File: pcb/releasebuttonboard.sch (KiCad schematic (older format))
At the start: 10 parts

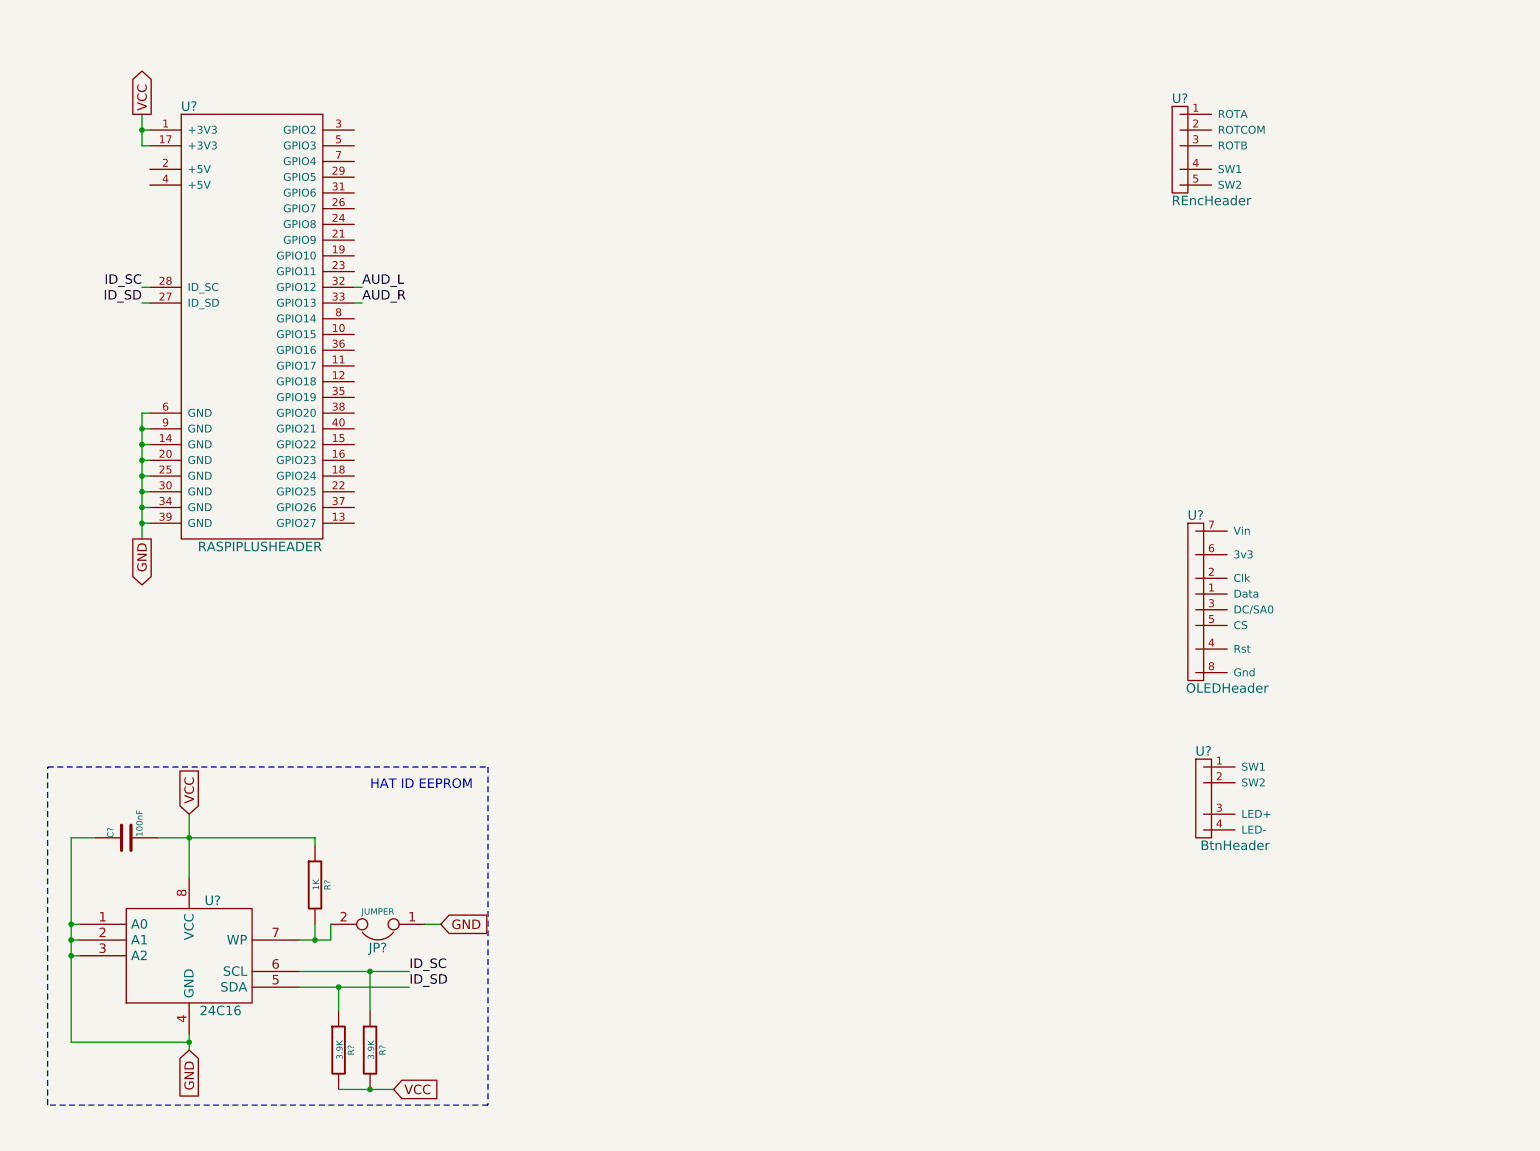
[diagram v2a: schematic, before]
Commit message: Audio output circuit.
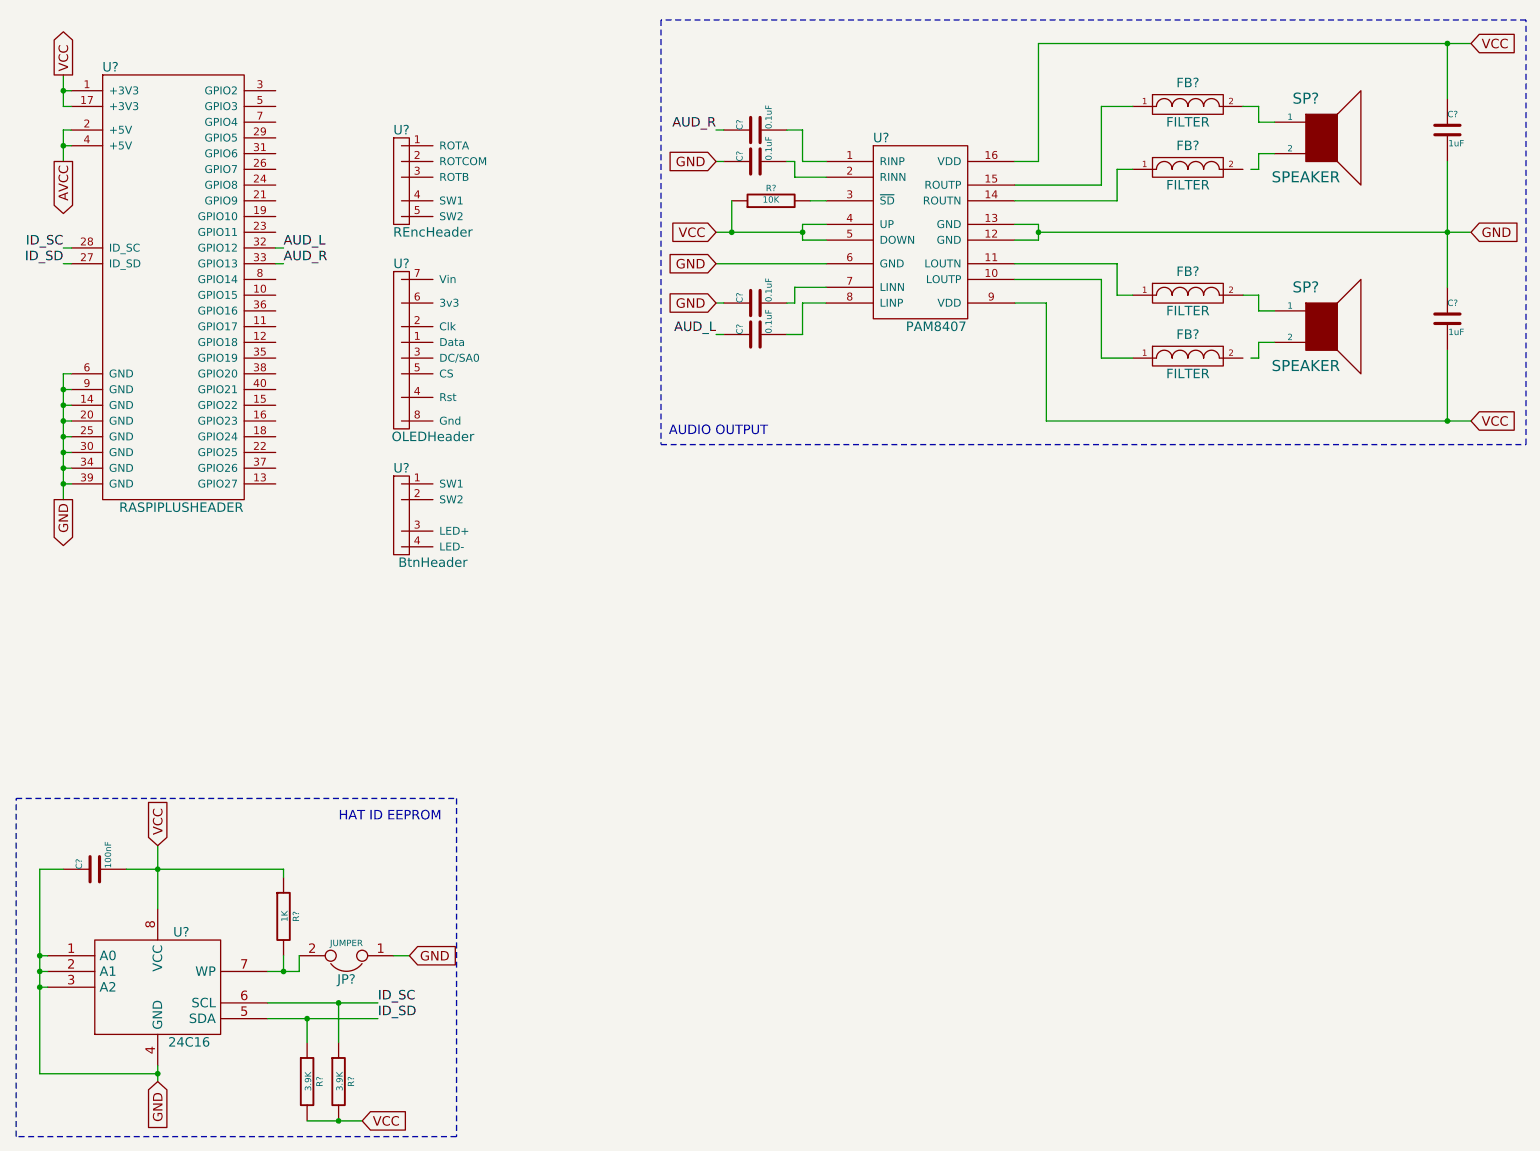
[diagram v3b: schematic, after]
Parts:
- added C? (x2): 1uF, symbol C
- added C? (x4): 0.1uF, symbol C
- added FB? (x4): FILTER, symbol FILTER
- added R?: 10K, symbol R
- added SP? (x2): SPEAKER, symbol SPEAKER
- added U?: PAM8407, symbol PAM8407
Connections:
- net AUD_L: now also C?.1
- net AUD_R: now also C?.1
- net GND: now also C?.1, C?.1, C?.1, C?.2, U?.12 (GND), U?.13 (GND), U?.6 (GND)
- net VCC: now also C?.1, C?.2, R?.1, U?.16 (VDD), U?.4 (UP), U?.5 (DOWN), U?.9 (VDD)
- net AVCC: now reaches U?.2 (+5V)
- net AVCC: now also U?.4 (+5V)
- new net: FB?.1, U?.15 (ROUTP)
- new net: FB?.2, SP?.1 (x2)
- new net: FB?.1, U?.14 (ROUTN)
- new net: C?.2, U?.1 (RINP)
- new net: FB?.1, U?.10 (LOUTP)
- new net: FB?.1, U?.11 (LOUTN)
- new net: C?.2, U?.2 (RINN)
- new net: R?.2, U?.3 (~SD)
- new net: C?.2, U?.7 (LINN)
- new net: C?.2, U?.8 (LINP)
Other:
- note added: "AUDIO OUTPUT"
- moved on the sheet: C?, JP?, R?, U?

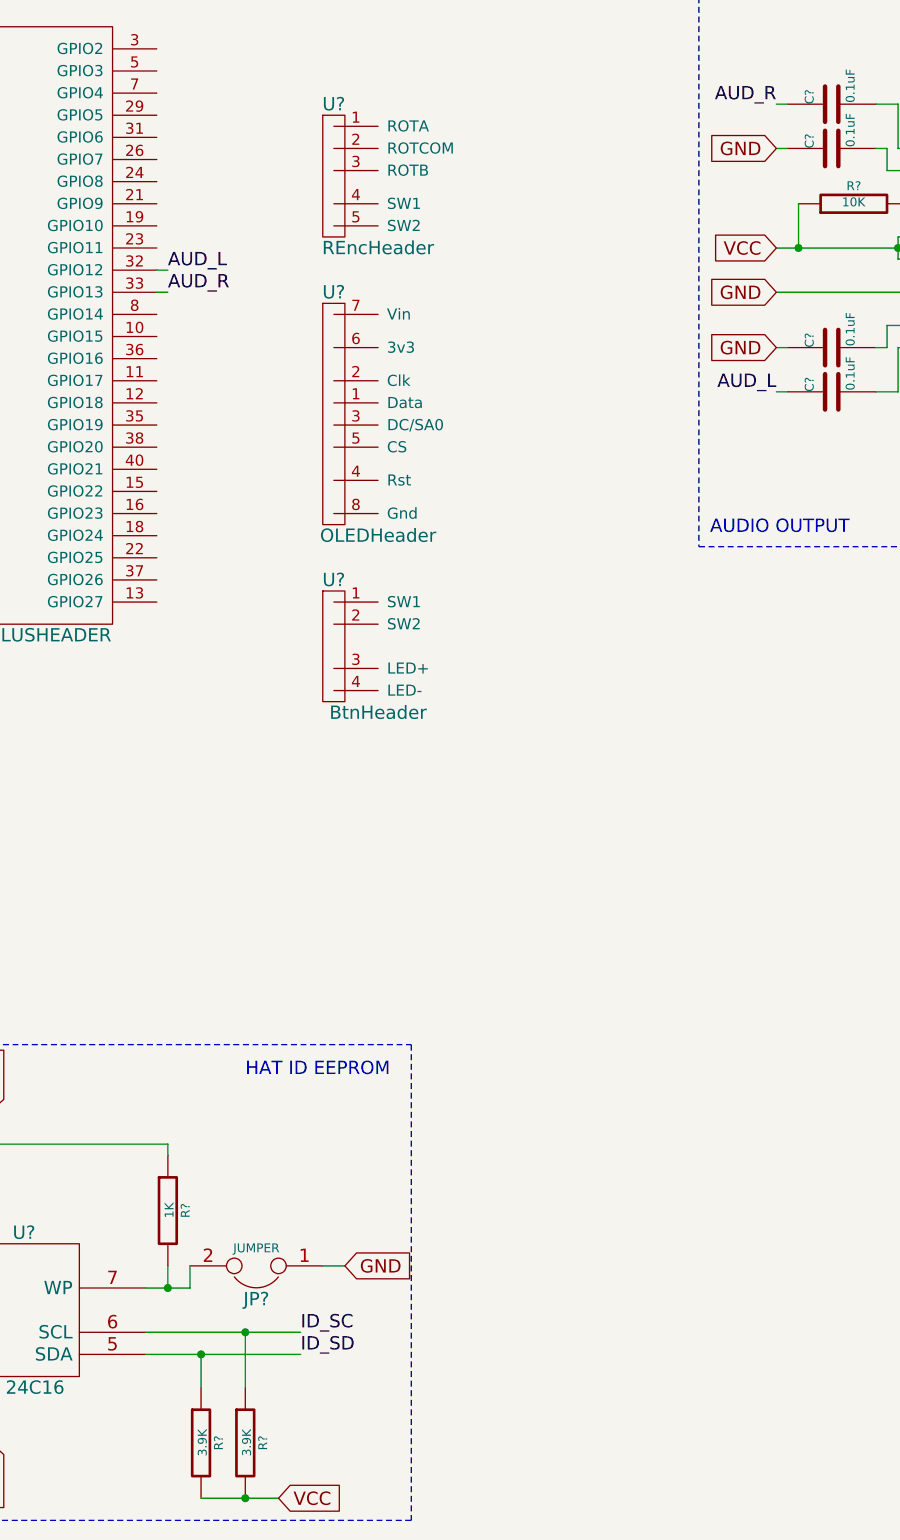
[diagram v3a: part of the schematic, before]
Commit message: Connect OLED header to Raspberry Pi IO pins.
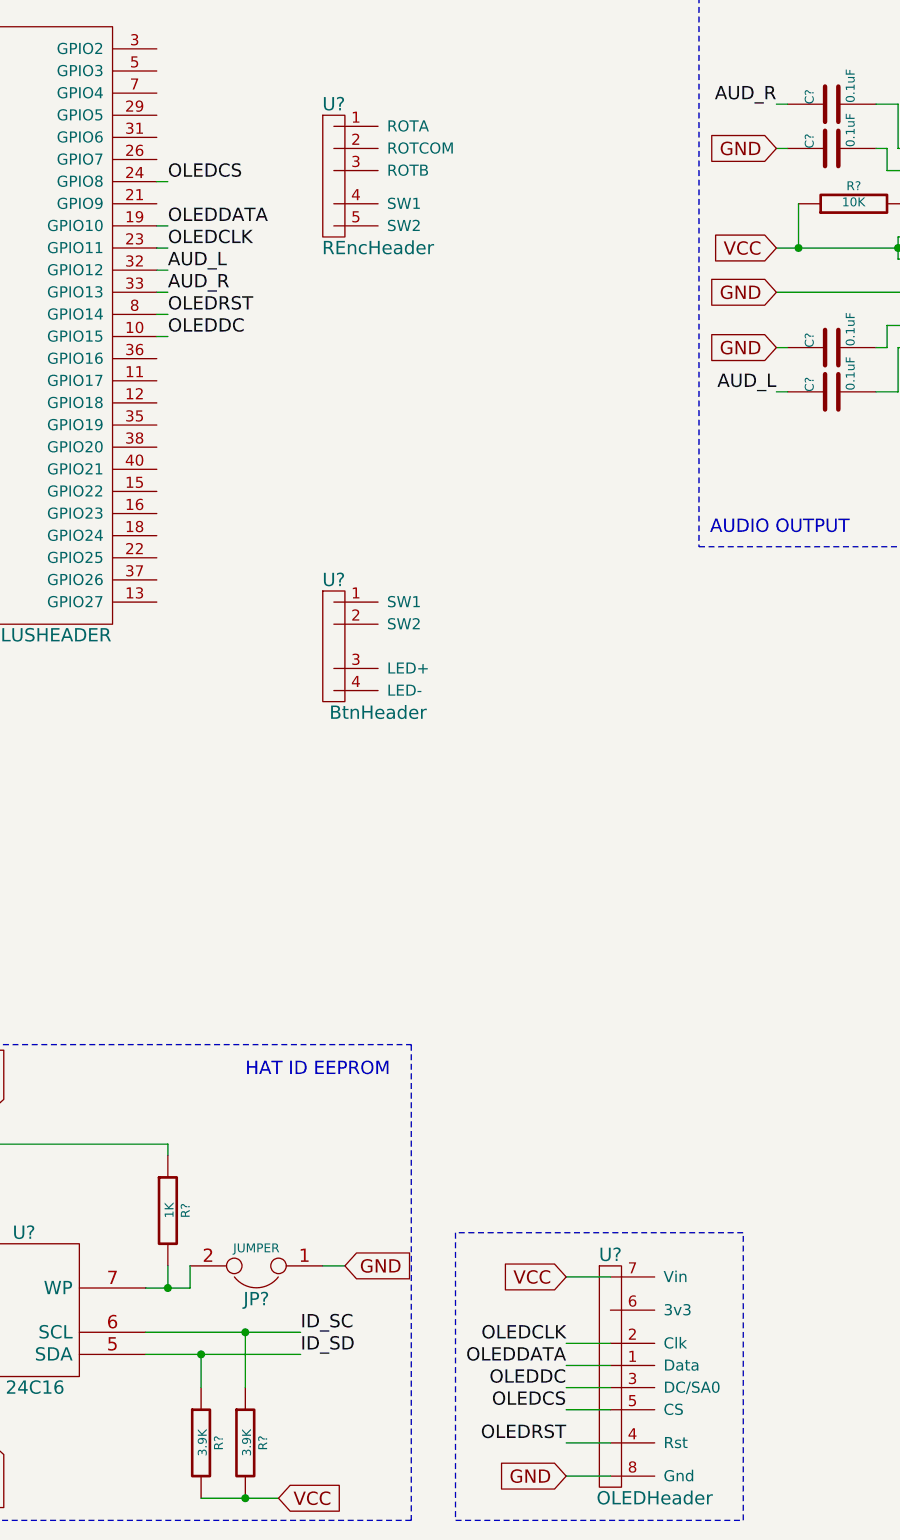
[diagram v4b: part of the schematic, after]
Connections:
- net GND: now also U?.8 (Gnd)
- net VCC: now also U?.7 (Vin)
- net OLEDDC: now reaches U?.10 (GPIO15)
- net OLEDDC: now also U?.3 (DC/SA0)
- net OLEDDATA: now reaches U?.19 (GPIO10)
- net OLEDDATA: now also U?.1 (Data)
- net OLEDCLK: now reaches U?.23 (GPIO11)
- net OLEDCLK: now also U?.2 (Clk)
- net OLEDCS: now reaches U?.24 (GPIO8)
- net OLEDCS: now also U?.5 (CS)
- net OLEDRST: now reaches U?.8 (GPIO14)
- net OLEDRST: now also U?.4 (Rst)
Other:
- moved on the sheet: U?
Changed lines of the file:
@@
 L OLEDHeader U?
 U 1 1 54A7A9C0
-P 3150 2750
-F 0 "U?" H 3150 3250 60  0000 C CNN
-F 1 "OLEDHeader" H 3350 2150 60  0000 C CNN
-F 2 "" H 3150 2950 60  0000 C CNN
-F 3 "" H 3150 2950 60  0000 C CNN
-	1    3150 2750
+P 4400 7100
+F 0 "U?" H 4400 7600 60  0000 C CNN
+F 1 "OLEDHeader" H 4600 6500 60  0000 C CNN
+F 2 "" H 4400 7300 60  0000 C CNN
+F 3 "" H 4400 7300 60  0000 C CNN
+	1    4400 7100
 	1    0    0    -1
 $EndComp
@@
 Text Notes 4850 3350 0    60   ~ 0
 AUDIO OUTPUT
+Text GLabel 4200 7600 0    60   Input ~ 0
+GND
+Text GLabel 4200 6700 0    60   Input ~ 0
+VCC
+Text Label 4200 7000 2    60   ~ 0
+OLEDCLK
+Text Label 4200 7100 2    60   ~ 0
+OLEDDATA
+Text Label 4200 7200 2    60   ~ 0
+OLEDDC
+Text Label 4200 7300 2    60   ~ 0
+OLEDCS
+Text Label 4200 7450 2    60   ~ 0
+OLEDRST
+Wire Wire Line
+	4200 6700 4400 6700
+Wire Wire Line
+	4200 7000 4400 7000
+Wire Wire Line
+	4200 7100 4400 7100
+Wire Wire Line
+	4200 7200 4400 7200
+Wire Wire Line
+	4200 7300 4400 7300
+Wire Wire Line
+	4200 7450 4400 7450
+Wire Wire Line
+	4200 7600 4400 7600
+Wire Notes Line
+	3700 6500 3700 7800
+Wire Notes Line
+	3700 7800 5000 7800
+Wire Notes Line
+	5000 7800 5000 6500
+Wire Notes Line
+	5000 6500 3700 6500
+Text Label 2400 1750 0    60   ~ 0
+OLEDCS
+Text Label 2400 2350 0    60   ~ 0
+OLEDRST
+Text Label 2400 2450 0    60   ~ 0
+OLEDDC
+Text Label 2400 2050 0    60   ~ 0
+OLEDCLK
+Text Label 2400 1950 0    60   ~ 0
+OLEDDATA
+Wire Wire Line
+	2350 1750 2400 1750
+Wire Wire Line
+	2350 1950 2400 1950
+Wire Wire Line
+	2350 2050 2400 2050
+Wire Wire Line
+	2350 2350 2400 2350
+Wire Wire Line
+	2350 2450 2400 2450
 $EndSCHEMATC

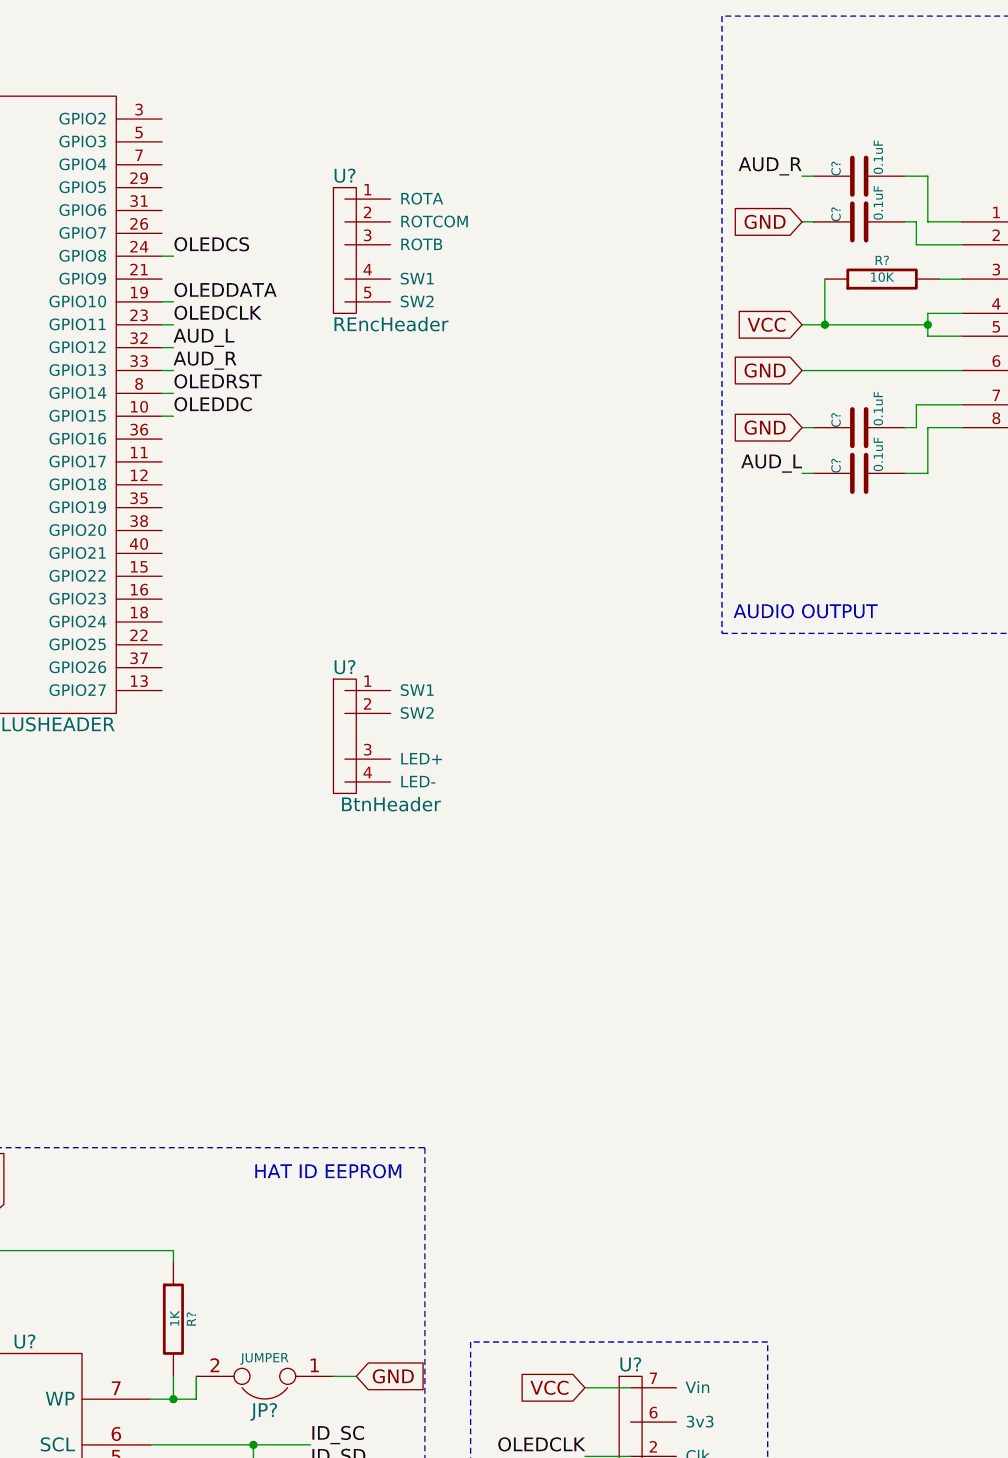
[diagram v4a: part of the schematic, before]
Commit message: Rotary encoder header connections.
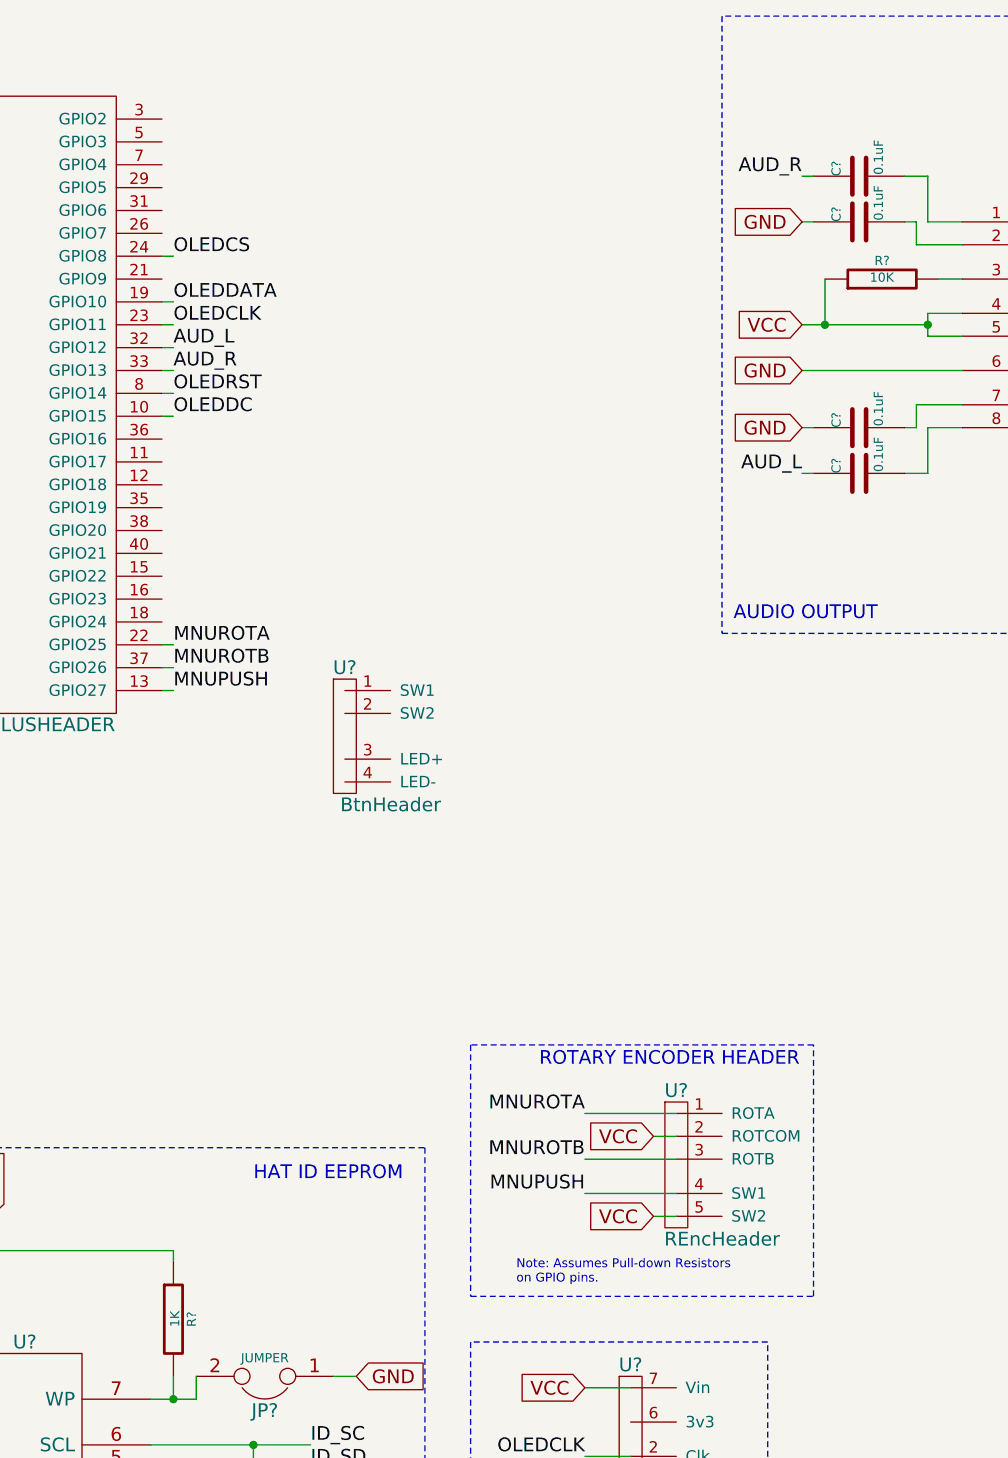
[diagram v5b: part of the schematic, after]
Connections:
- net VCC: now also U?.2 (ROTCOM), U?.5 (SW2)
- net MNUPUSH: now reaches U?.13 (GPIO27)
- net MNUPUSH: now also U?.4 (SW1)
- net MNUROTA: now reaches U?.22 (GPIO25)
- net MNUROTA: now also U?.1 (ROTA)
- net MNUROTB: now reaches U?.37 (GPIO26)
- net MNUROTB: now also U?.3 (ROTB)
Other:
- note added: "Note: Assumes Pull-down Resistors\non GPIO pins."
- note added: "ROTARY ENCODER HEADER"
- moved on the sheet: U?
